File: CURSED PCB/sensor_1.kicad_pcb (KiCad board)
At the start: 4 copper layers, 42 x 40 mm, 83 parts, among them J1 Debugging Connector, J2 Micro_SD_Card, J3 Gecko Connector, J5 G125-MH104M4-04AD000P, U1 STM32G431KBT6, U10 MCP2562, U12 AD5761BRUZ, U2 INA180-A3, U3 MIC94090YC6, U4 SPX3819M5-L-3-3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

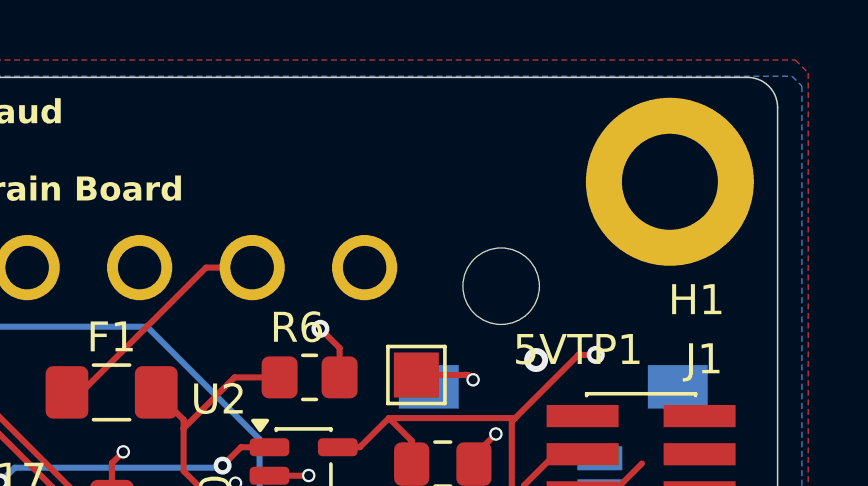
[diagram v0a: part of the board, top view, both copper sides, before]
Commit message: added a warning label
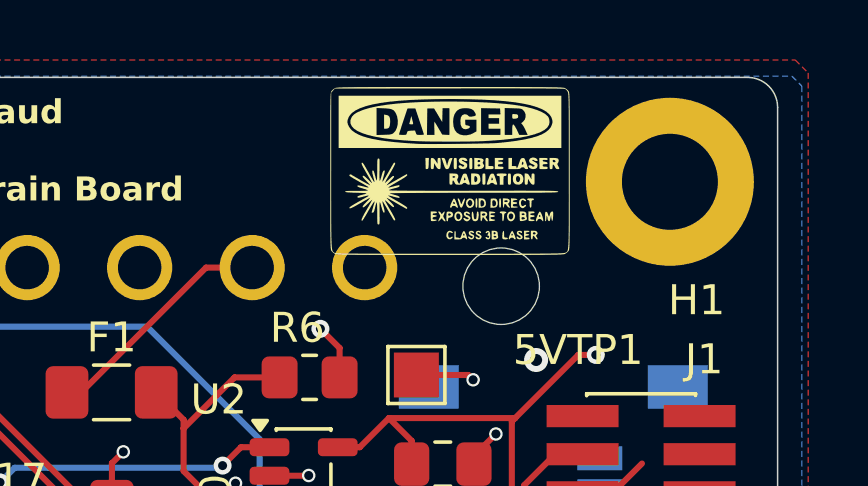
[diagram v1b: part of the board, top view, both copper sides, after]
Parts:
- added G***: LOGO, LOGO, F.Cu at (60.7, 32.6)
- added G***: LOGO, LOGO, B.Cu at (50.3, 40.9)

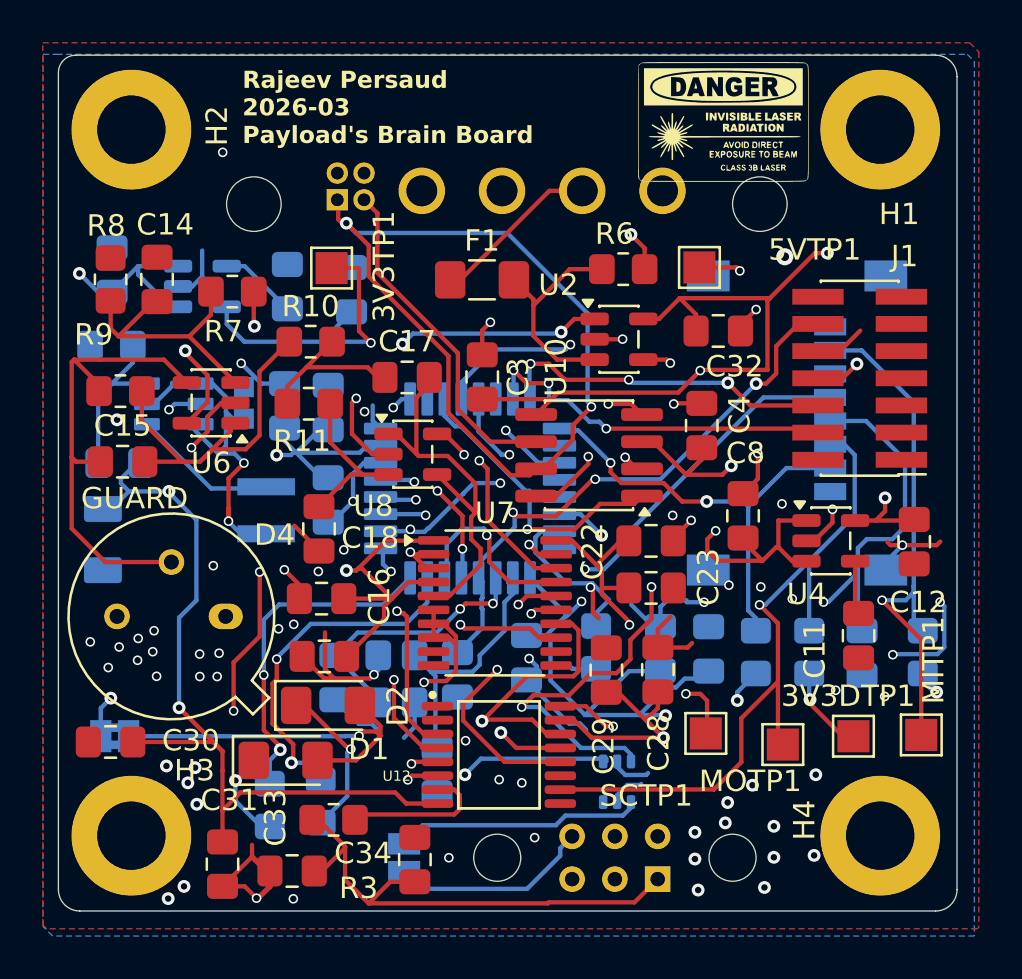
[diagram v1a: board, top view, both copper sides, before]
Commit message: fixed some odd looking vias
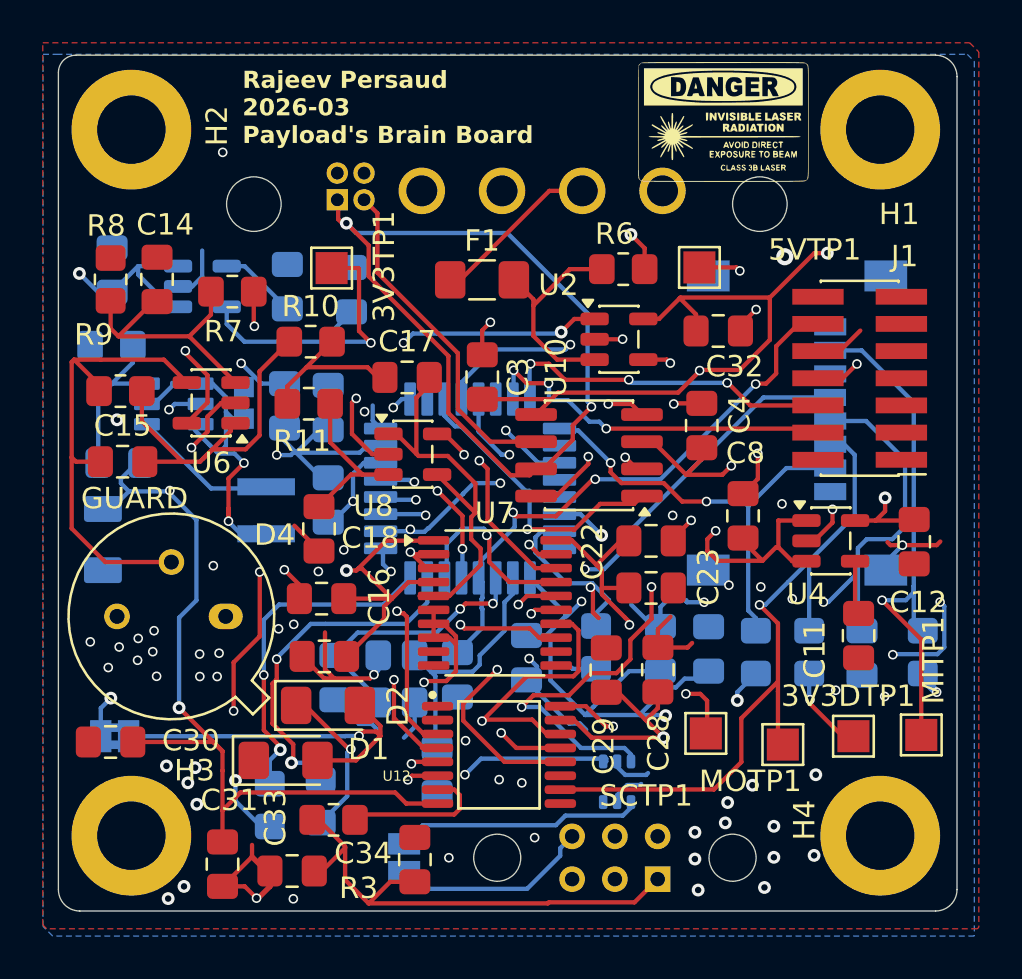
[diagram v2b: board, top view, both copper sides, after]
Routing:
- net +3.3VD: track 131.6 -> 130.8 mm

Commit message: fixed cursense
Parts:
- moved 5VTP1 9.56 mm to (50.1, 41.1)
- moved R6 2.84 mm to (53.4, 40.8), turned to -90 degrees
- moved U2 2.25 mm to (56.4, 40.6), turned to -90 degrees
- moved C32 1.84 mm to (59.4, 40.9), turned to 90 degrees
- moved F1 1.43 mm to (49.4, 38.6)
- moved C3 0.14 mm to (49.5, 44.6)
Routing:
- net /CUR_SEN: track 22.5 -> 28.7 mm
- net Net-(U2-+): track 10.2 -> 5.67 mm
- net Net-(J5-+5V): track 7.90 -> 11.6 mm
- net +3.3VD: track 130.8 -> 127.9 mm
- net +5V: track 77.8 -> 78.9 mm, vias 13 -> 11
- net GND: track 120.0 -> 120.9 mm, vias 79 -> 80

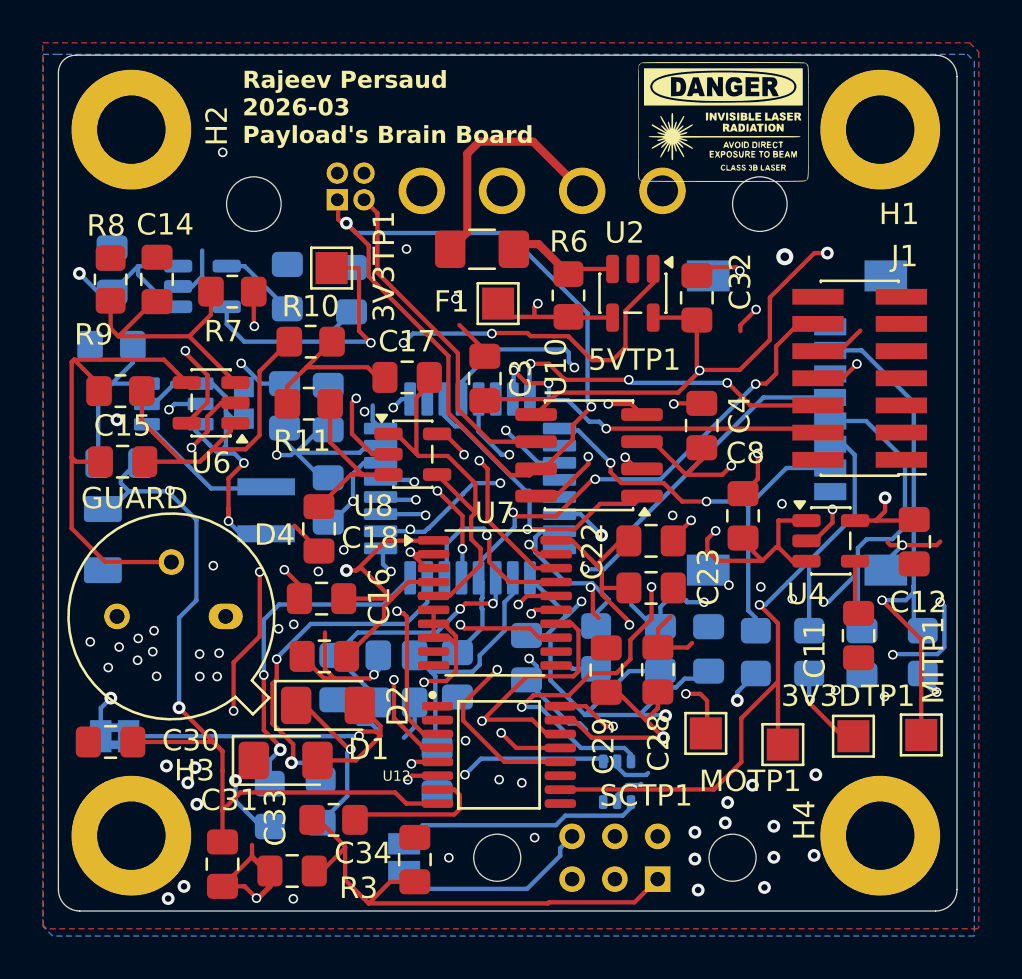
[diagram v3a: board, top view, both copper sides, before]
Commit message: small traces redoes
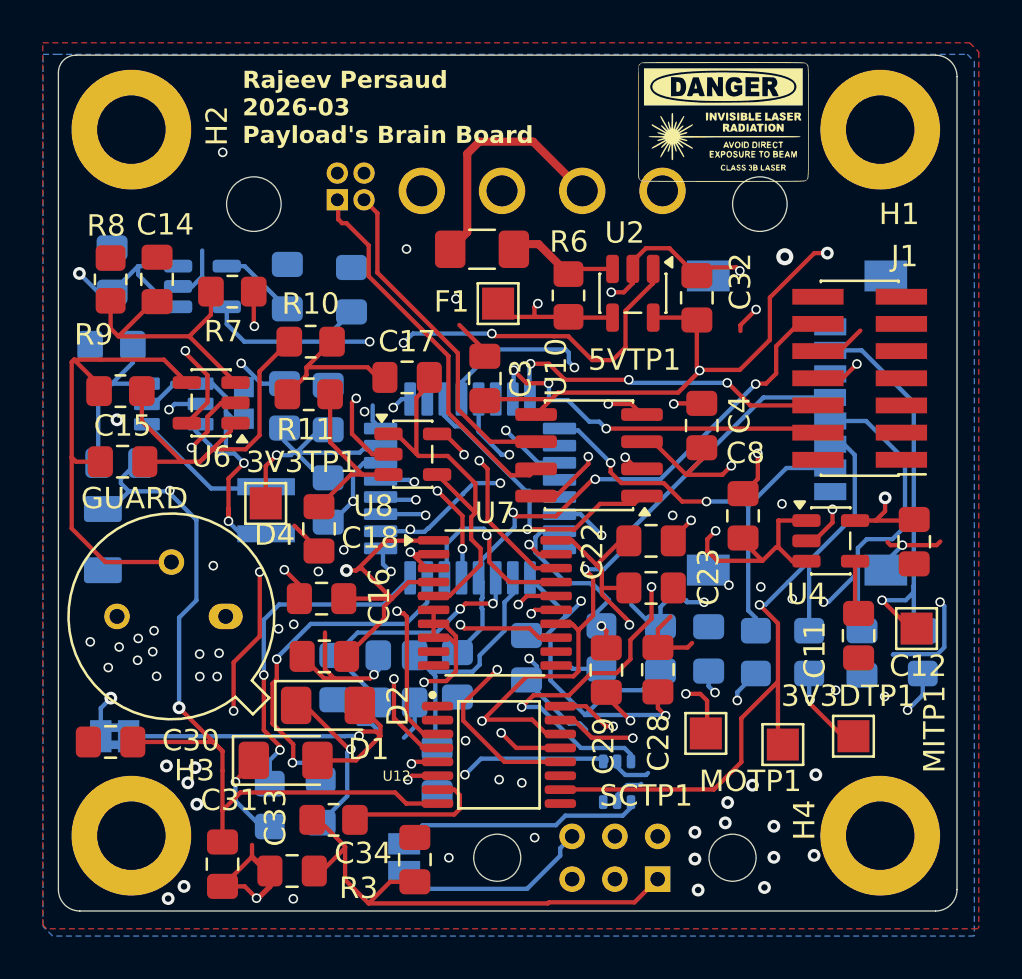
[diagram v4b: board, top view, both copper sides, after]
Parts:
- moved 3V3TP1 11.4 mm to (39.3, 50.5)
- moved MITP1 4.97 mm to (69.7, 56.3)
- moved R11 0.44 mm to (41.3, 45.4)
- moved R15 0.25 mm to (55.0, 57.2)
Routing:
- net /Power/CANH: track 39.3 -> 18.0 mm, vias 2 -> 0
- net /SCLK: track 64.4 -> 55.8 mm
- net /MISO: track 65.3 -> 60.2 mm
- net GND: track 120.9 -> 125.6 mm
- net +3.3VD: track 127.9 -> 123.5 mm, vias 15 -> 17

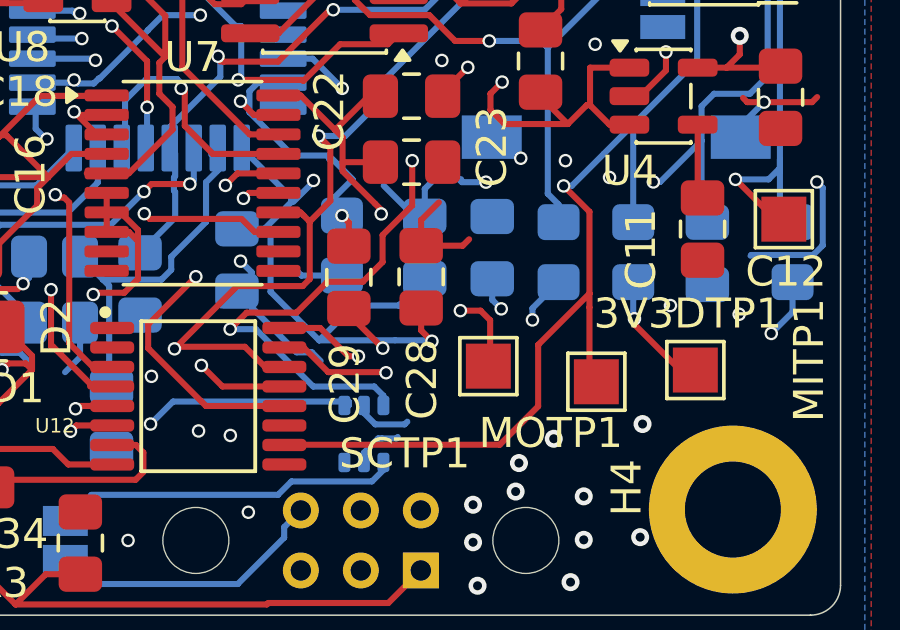
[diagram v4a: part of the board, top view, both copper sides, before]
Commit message: moved warning label slighty
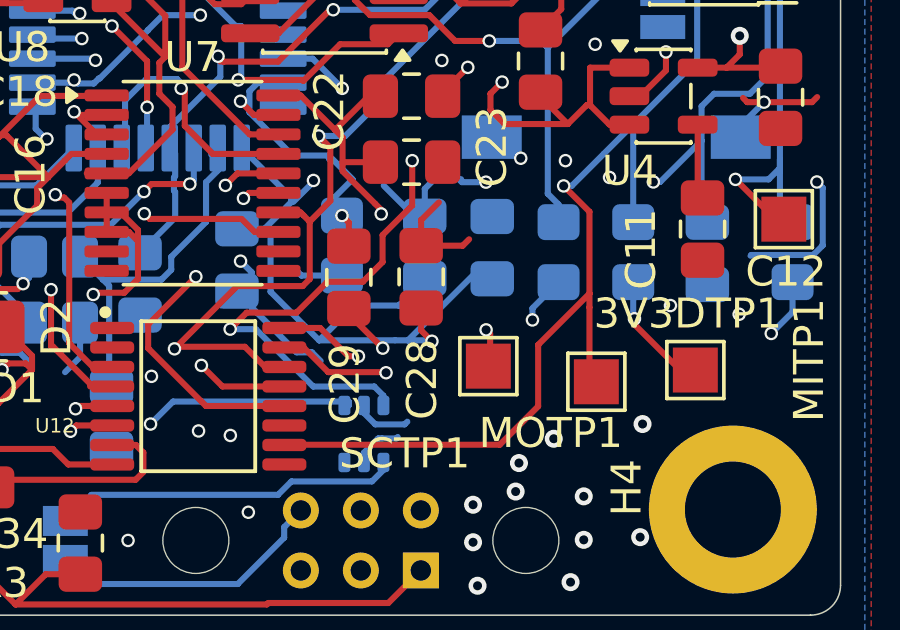
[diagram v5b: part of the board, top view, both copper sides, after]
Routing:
- net +3.3VD: track 123.5 -> 126.1 mm, vias 17 -> 16
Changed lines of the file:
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@@
-	)
-	(via
-		(at 60.279626 59.310374)
-		(size 0.45)
-		(drill 0.3)
-		(layers "F.Cu" "B.Cu")
-		(net 6)
 	)
 	(via
@@
 	)
 	(segment
+		(start 59.4 58.13)
+		(end 57.17 60.36)
+		(width 0.2032)
+		(layer "B.Cu")
+		(net 6)
+	)
+	(segment
 		(start 55.37 59.2)
 		(end 54.21 60.36)
@@
 	)
 	(segment
-		(start 59.98 58.3075)
-		(end 59.98 59.010748)
-		(width 0.2032)
-		(layer "B.Cu")
-		(net 6)
-	)
-	(segment
 		(start 69.1615 51.5485)
 		(end 69.1615 48.44)
@@
 	)
 	(segment
+		(start 56.74 60.36)
+		(end 57.17 60.36)
+		(width 0.2032)
+		(layer "B.Cu")
+		(net 6)
+	)
+	(segment
 		(start 65.6631 46.6166)
 		(end 66.3347 46.6166)
@@
 	)
 	(segment
+		(start 59.98 58.13)
+		(end 59.4 58.13)
+		(width 0.2032)
+		(layer "B.Cu")
+		(net 6)
+	)
+	(segment
 		(start 57.94 60.36)
 		(end 57.97 60.39)
@@
 	)
 	(segment
-		(start 56.74 60.36)
+		(start 57.17 60.36)
 		(end 57.94 60.36)
 		(width 0.2032)
@@
 		(start 69.1615 48.44)
 		(end 67.3381 46.6166)
-		(width 0.2032)
-		(layer "B.Cu")
-		(net 6)
-	)
-	(segment
-		(start 59.98 59.010748)
-		(end 60.279626 59.310374)
 		(width 0.2032)
 		(layer "B.Cu")
@@
 	)
 	(segment
-		(start 58.9175 59.37)
-		(end 59.59 59.37)
-		(width 0.2032)
-		(layer "F.Cu")
-		(net 16)
-	)
-	(segment
-		(start 59.59 59.37)
-		(end 59.91 59.69)
-		(width 0.2032)
-		(layer "F.Cu")
-		(net 16)
-	)
-	(segment
 		(start 53.8958 58.31586)
 		(end 53.66086 58.5508)
@@
 	)
 	(segment
+		(start 59.775 60.01)
+		(end 59.91 60.145)
+		(width 0.2032)
+		(layer "F.Cu")
+		(net 16)
+	)
+	(segment
 		(start 53.66086 58.5508)
 		(end 51.480042 58.5508)
@@
 	)
 	(segment
-		(start 59.91 59.69)
-		(end 59.91 60.9)
-		(width 0.2032)
-		(layer "F.Cu")
-		(net 16)
-	)
-	(segment
 		(start 53.589999 56.095)
 		(end 53.6875 56.1925)
@@
 	)
 	(segment
+		(start 59.91 60.145)
+		(end 59.91 60.9)
+		(width 0.2032)
+		(layer "F.Cu")
+		(net 16)
+	)
+	(segment
 		(start 49.387642 60.6432)
 		(end 49.456642 60.5742)
@@
 	)
 	(via
-		(at 58.9175 59.37)
+		(at 59.775 60.01)
 		(size 0.45)
 		(drill 0.3)
@@
 	(segment
 		(start 50.62 59.410842)
-		(end 58.876658 59.410842)
+		(end 49.387642 60.6432)
+		(width 0.2032)
+		(layer "In2.Cu")
+		(net 16)
+	)
+	(segment
+		(start 58.876658 59.410842)
+		(end 50.62 59.410842)
+		(width 0.2032)
+		(layer "In2.Cu")
+		(net 16)
+	)
+	(segment
+		(start 59.775 60.01)
+		(end 59.475816 60.01)
 		(width 0.2032)
 		(layer "In2.Cu")
@@
 	)
 	(segment
-		(start 50.62 59.410842)
-		(end 49.387642 60.6432)
-		(width 0.2032)
-		(layer "In2.Cu")
-		(net 16)
-	)
-	(segment
 		(start 50.722482 50.020951)
 		(end 50.722482 49.992482)
@@
 	)
 	(segment
-		(start 58.876658 59.410842)
-		(end 58.9175 59.37)
-		(width 0.2032)
-		(layer "In2.Cu")
-		(net 16)
-	)
-	(segment
 		(start 46.01 51.68)
 		(end 46.04 51.68)
 		(width 0.2032)
 		(layer "In2.Cu")
+		(net 16)
+	)
+	(segment
+		(start 59.475816 60.01)
+		(end 58.876658 59.410842)
+		(width 0.2032)
+		(layer "In2.Cu")

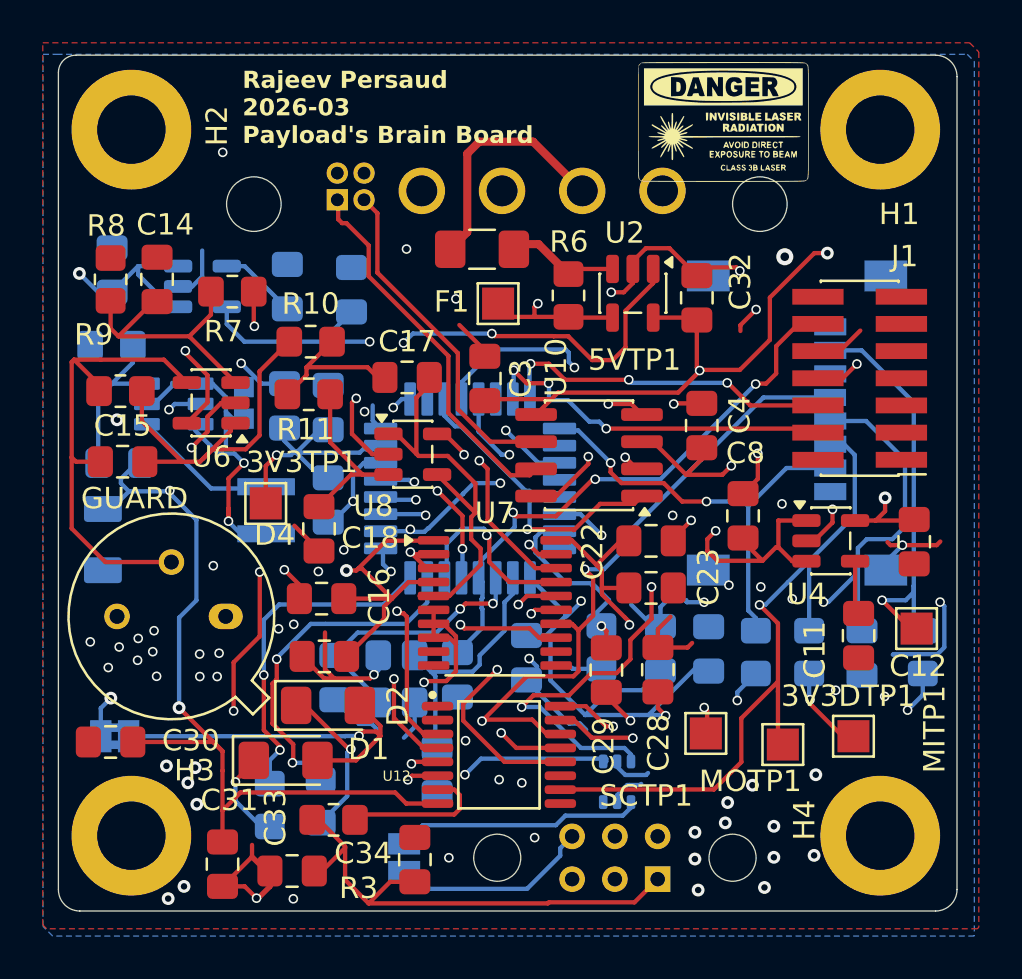
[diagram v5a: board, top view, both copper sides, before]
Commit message: cleaned up a a long trace
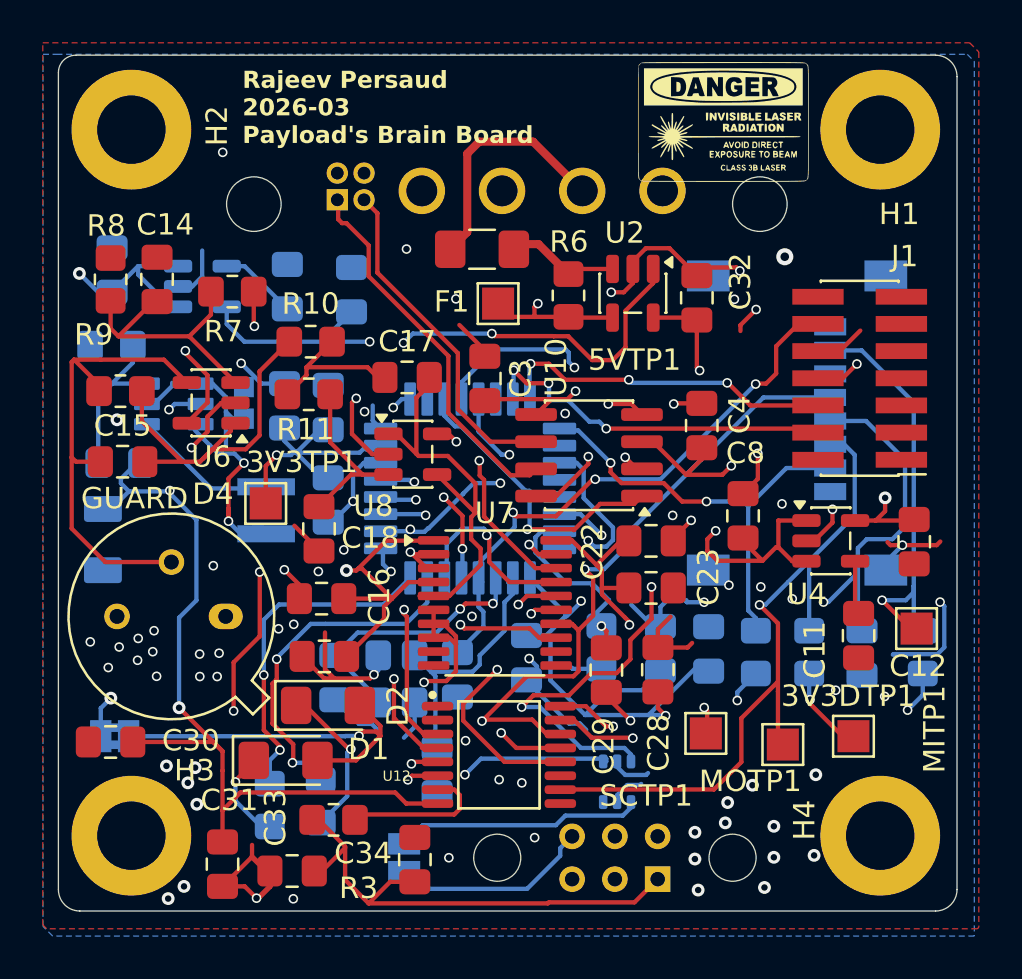
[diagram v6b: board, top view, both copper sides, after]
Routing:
- net +5V: track 78.9 -> 102.7 mm, vias 11 -> 12
- net +3.3VD: track 126.1 -> 103.0 mm, vias 16 -> 17
- net /MCU/CS_DAC: track 20.1 -> 18.2 mm
- net /MCU/DAC_RESET: track 23.7 -> 24.9 mm, vias 2 -> 3

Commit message: last change trust
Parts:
- L1: value 12uH -> 10uH
- R12: value 120k -> 71.5K
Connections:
- C2 pad 1: /MCU/OCS2/CLKOUT -> GND
- C2 pad 2: GND -> /MCU/OCS2/CLKOUT
- R15 pad 1: GND -> Net-(U1-PB8-BOOT0)
- U1 pad 31: GND -> Net-(U1-PB8-BOOT0)
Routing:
- net Net-(U1-PB8-BOOT0): track 0.00 -> 8.81 mm, vias 0 -> 2
- net +5V: track 102.7 -> 108.8 mm
- net GND: track 125.6 -> 119.9 mm, vias 80 -> 84
- net /MCU/Las_enable: track 21.9 -> 24.9 mm, vias 3 -> 2
- net +3.3VD: track 103.0 -> 101.8 mm
- net /SCLK: track 55.5 -> 56.7 mm, vias 5 -> 6
- net /MCU/OCS2/CLKOUT: track 12.7 -> 13.5 mm
- net /MCU/DAC_RESET: track 24.9 -> 24.1 mm
- net /MCLR: track 26.9 -> 27.6 mm

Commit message: commit for pranav
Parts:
- removed C18: 43nF, Capacitor_SMD:C_0805_2012Metric_Pad1.18x1.45mm_HandSolder
- moved G*** 0.23 mm to (50.3, 40.7)
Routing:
- net +5V: track 108.8 -> 89.9 mm
- net /SCLK: track 56.7 -> 53.4 mm
- net GND: track 119.9 -> 117.1 mm, vias 84 -> 85
- net /MKLKIN: track 12.0 -> 13.7 mm
- net /MCLR: track 27.6 -> 26.5 mm
- net /MCU/CS_DAC: track 18.2 -> 19.1 mm
- net +3.3VA: track 65.4 -> 64.6 mm
